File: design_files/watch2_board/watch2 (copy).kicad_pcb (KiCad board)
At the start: 2 copper layers, 48.6 x 42.9 mm, 74 parts, among them J1 USB_C_Receptacle_USB2.0, J2 STEMMA QT, J3 UART Connector, J4 Conn_01x03_Male, J5 Conn_01x03_Male, J6 TFT Connector, J7 Torch Connector (main board), J8 Torch Connector (daughter boa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, Q1 Q_NPN_BCE, Q2 Q_NPN_BCE, Q3 Q_NPN_BCE, SW2 SW_Push, U1 FT230XS, U2 MCP73831-2-OT, U3 MAX17043G+U, U4 MAX16150AUT+T, U5 MAX604, U6 MCP23008-xSS, U7 ESP32-WROVER, U8 MAX98357AETE+T, U9 TSOP38238

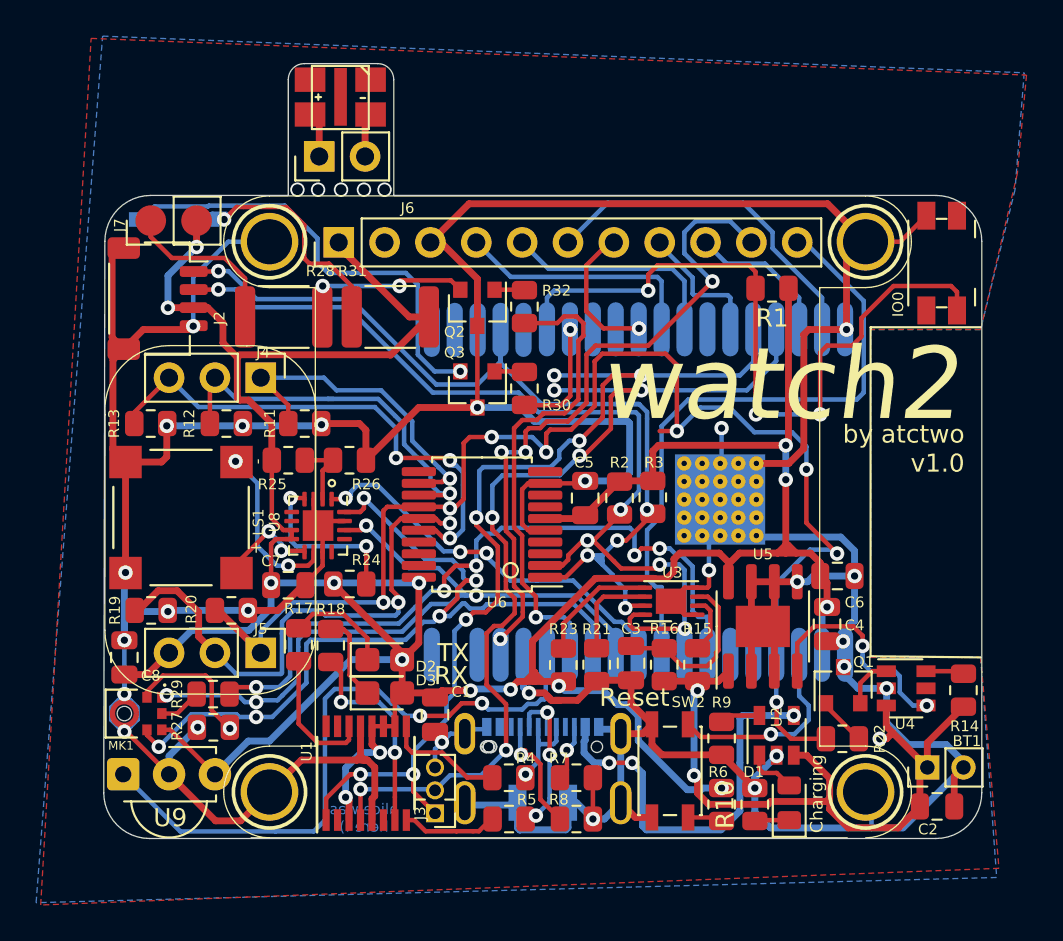
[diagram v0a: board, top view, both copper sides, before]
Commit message: created initial version of the pcb
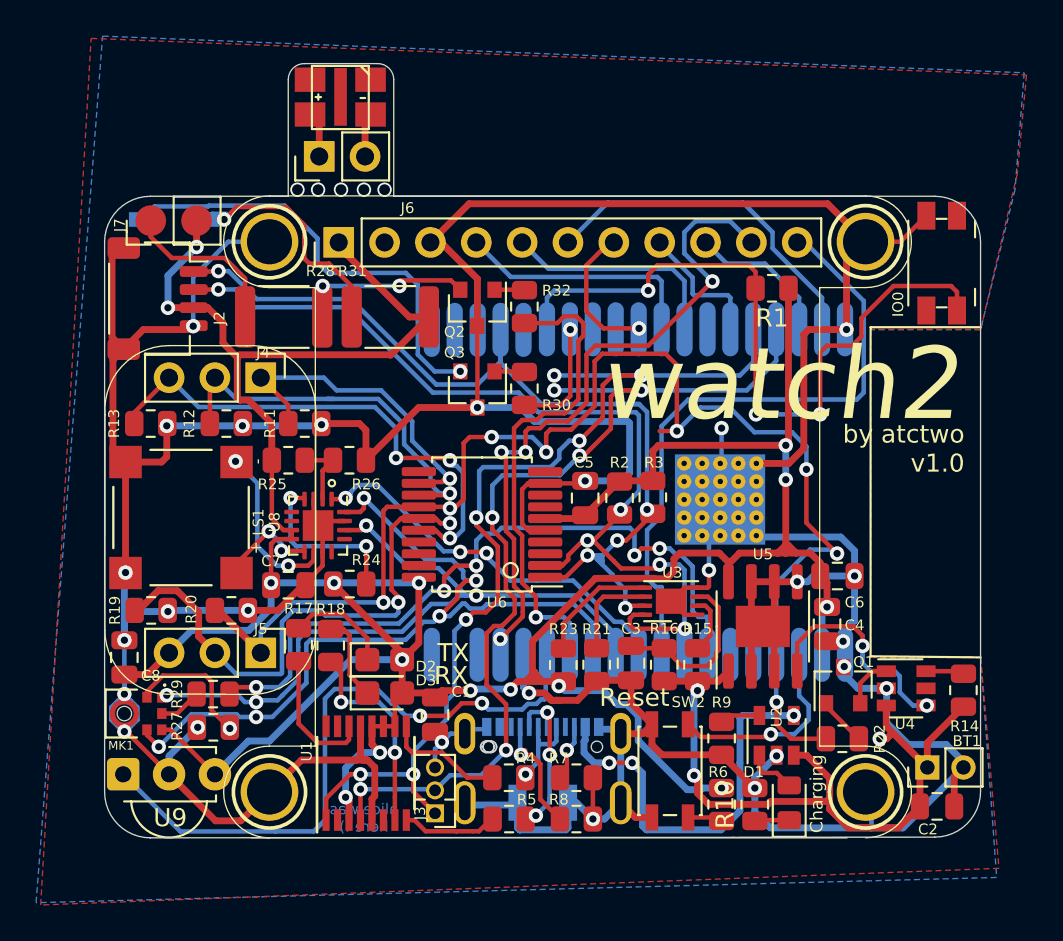
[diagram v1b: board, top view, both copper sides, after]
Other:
- board size 48.6 x 42.9 mm -> 48.5 x 42.9 mm
- copper layers 2 -> 16
